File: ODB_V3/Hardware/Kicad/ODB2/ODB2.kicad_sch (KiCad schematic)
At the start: 95 parts, among them U1 STM32F412ZGTx, Y1 ABM8G-25.000MHZ-18-D2Y-T

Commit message: wip: route qspi
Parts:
- BARO_R1, BARO_R2, BARO_R3, BT_R3, Crystal_R1, EXTEND_R1, EXTEND_R10, EXTEND_R11, EXTEND_R2, EXTEND_R3, EXTEND_R4, EXTEND_R5, EXTEND_R6, EXTEND_R7, EXTEND_R8, EXTEND_R9, GPS_R1, IMU_R5, MEM_R1, MEM_R2, MEM_R3, MEM_R4, MEM_R5, MEM_R6, PA_R6, P_R21, P_R22, P_R23, P_R24, RFD_R1, SD_R1, SD_R2, SD_R3: footprint Resistor_SMD:R_0603_1608Metric -> Resistor_SMD:R_0402_1005Metric
- Crystal_C1, Crystal_C2: footprint Capacitor_SMD:C_0603_1608Metric -> Capacitor_SMD:C_0402_1005Metric
- Crystal_R2: value 1MHz -> 1M; footprint Resistor_SMD:R_0603_1608Metric -> Resistor_SMD:R_0402_1005Metric
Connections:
- net PH1: no longer Crystal_R2.2
- net at Crystal_C2.1, Crystal_R1.2, Y1.3: now also Crystal_R2.2
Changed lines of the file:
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@@
 	)
 	(junction
-		(at 391.16 127)
-		(diameter 0)
-		(color 0 0 0 0)
-	)
-	(junction
 		(at 210.82 44.45)
 		(diameter 0)
@@
 	)
 	(junction
+		(at 384.81 139.7)
+		(diameter 0)
+		(color 0 0 0 0)
+	)
+	(junction
 		(at 360.68 101.6)
 		(diameter 0)
@@
 	(wire
 		(pts
-			(xy 391.16 125.73) (xy 391.16 127)
-		)
-		(stroke
-			(width 0)
-			(type default)
-		)
-	)
-	(wire
-		(pts
 			(xy 147.32 213.36) (xy 147.32 218.44)
 		)
@@
 	(wire
 		(pts
-			(xy 381 139.7) (xy 391.16 139.7)
+			(xy 381 139.7) (xy 384.81 139.7)
 		)
 		(stroke
@@
 	(wire
 		(pts
-			(xy 364.49 127) (xy 391.16 127)
-		)
-		(stroke
-			(width 0)
-			(type default)
-		)
-	)
-	(wire
-		(pts
 			(xy 147.32 55.88) (xy 147.32 57.15)
 		)
@@
 	(wire
 		(pts
+			(xy 384.81 139.7) (xy 391.16 139.7)
+		)
+		(stroke
+			(width 0)
+			(type default)
+		)
+	)
+	(wire
+		(pts
+			(xy 364.49 127) (xy 384.81 127)
+		)
+		(stroke
+			(width 0)
+			(type default)
+		)
+	)
+	(wire
+		(pts
 			(xy 365.76 26.67) (xy 365.76 31.75)
 		)
@@
 	(wire
 		(pts
-			(xy 391.16 127) (xy 391.16 129.54)
+			(xy 391.16 125.73) (xy 391.16 129.54)
 		)
 		(stroke
@@
 	(wire
 		(pts
+			(xy 384.81 127) (xy 384.81 139.7)
+		)
+		(stroke
+			(width 0)
+			(type default)
+		)
+	)
+	(wire
+		(pts
 			(xy 388.62 31.75) (xy 388.62 34.29)
 		)
@@
 			)
 		)
-		(property "Footprint" "Resistor_SMD:R_0603_1608Metric"
+		(property "Footprint" "Resistor_SMD:R_0402_1005Metric"
 			(at 163.83 158.242 90)
 			(effects
@@
 			)
 		)
-		(property "Footprint" "Resistor_SMD:R_0603_1608Metric"
+		(property "Footprint" "Resistor_SMD:R_0402_1005Metric"
 			(at 238.76 189.738 90)
 			(effects
@@
 			)
 		)
-		(property "Footprint" "Resistor_SMD:R_0603_1608Metric"
+		(property "Footprint" "Resistor_SMD:R_0402_1005Metric"
 			(at 163.83 160.782 90)
 			(effects
@@
 			)
 		)
-		(property "Footprint" "Resistor_SMD:R_0603_1608Metric"
+		(property "Footprint" "Resistor_SMD:R_0402_1005Metric"
 			(at 237.49 70.358 90)
 			(effects
@@
 			)
 		)
-		(property "Footprint" "Resistor_SMD:R_0603_1608Metric"
+		(property "Footprint" "Resistor_SMD:R_0402_1005Metric"
 			(at 238.76 199.898 90)
 			(effects
@@
 			)
 		)
-		(property "Value" "1MHz"
+		(property "Value" "1M"
 			(at 360.68 124.714 90)
 			(effects
@@
 			)
 		)
-		(property "Footprint" "Resistor_SMD:R_0603_1608Metric"
+		(property "Footprint" "Resistor_SMD:R_0402_1005Metric"
 			(at 360.68 128.778 90)
 			(effects
@@
 			)
 		)
-		(property "Footprint" "Resistor_SMD:R_0603_1608Metric"
+		(property "Footprint" "Resistor_SMD:R_0402_1005Metric"
 			(at 237.49 113.538 90)
 			(effects
@@
 			)
 		)
-		(property "Footprint" "Resistor_SMD:R_0603_1608Metric"
+		(property "Footprint" "Resistor_SMD:R_0402_1005Metric"
 			(at 163.83 163.322 90)
 			(effects
@@
 			)
 		)
-		(property "Footprint" "Resistor_SMD:R_0603_1608Metric"
+		(property "Footprint" "Resistor_SMD:R_0402_1005Metric"
 			(at 237.49 75.438 90)
 			(effects
@@
 			)
 		)
-		(property "Footprint" "Resistor_SMD:R_0603_1608Metric"
+		(property "Footprint" "Resistor_SMD:R_0402_1005Metric"
 			(at 237.49 159.258 90)
 			(effects
@@
 			)
 		)
-		(property "Footprint" "Resistor_SMD:R_0603_1608Metric"
+		(property "Footprint" "Resistor_SMD:R_0402_1005Metric"
 			(at 163.83 196.342 90)
 			(effects
@@
 			)
 		)
-		(property "Footprint" "Capacitor_SMD:C_0603_1608Metric"
+		(property "Footprint" "Capacitor_SMD:C_0402_1005Metric"
 			(at 333.7052 144.78 0)
 			(effects
@@
 			)
 		)
-		(property "Footprint" "Capacitor_SMD:C_0603_1608Metric"
+		(property "Footprint" "Capacitor_SMD:C_0402_1005Metric"
 			(at 392.1252 148.59 0)
 			(effects
@@
 			)
 		)
-		(property "Footprint" "Resistor_SMD:R_0603_1608Metric"
+		(property "Footprint" "Resistor_SMD:R_0402_1005Metric"
 			(at 238.76 212.598 90)
 			(effects
@@
 			)
 		)
-		(property "Footprint" "Resistor_SMD:R_0603_1608Metric"
+		(property "Footprint" "Resistor_SMD:R_0402_1005Metric"
 			(at 163.83 148.082 90)
 			(effects
@@
 			)
 		)
-		(property "Footprint" "Resistor_SMD:R_0603_1608Metric"
+		(property "Footprint" "Resistor_SMD:R_0402_1005Metric"
 			(at 163.83 140.462 90)
 			(effects
@@
 			)
 		)
-		(property "Footprint" "Resistor_SMD:R_0603_1608Metric"
+		(property "Footprint" "Resistor_SMD:R_0402_1005Metric"
 			(at 237.49 138.938 90)
 			(effects
@@
 			)
 		)
-		(property "Footprint" "Resistor_SMD:R_0603_1608Metric"
+		(property "Footprint" "Resistor_SMD:R_0402_1005Metric"
 			(at 237.49 62.738 90)
 			(effects
@@
 			)
 		)
-		(property "Footprint" "Resistor_SMD:R_0603_1608Metric"
+		(property "Footprint" "Resistor_SMD:R_0402_1005Metric"
 			(at 389.382 133.35 90)
 			(effects
@@
 			)
 		)
-		(property "Footprint" "Resistor_SMD:R_0603_1608Metric"
+		(property "Footprint" "Resistor_SMD:R_0402_1005Metric"
 			(at 238.76 210.058 90)
 			(effects
@@
 			)
 		)
-		(property "Footprint" "Resistor_SMD:R_0603_1608Metric"
+		(property "Footprint" "Resistor_SMD:R_0402_1005Metric"
 			(at 163.83 82.042 90)
 			(effects
@@
 			)
 		)
-		(property "Footprint" "Resistor_SMD:R_0603_1608Metric"
+		(property "Footprint" "Resistor_SMD:R_0402_1005Metric"
 			(at 163.83 143.002 90)
 			(effects
@@
 			)
 		)
-		(property "Footprint" "Resistor_SMD:R_0603_1608Metric"
+		(property "Footprint" "Resistor_SMD:R_0402_1005Metric"
 			(at 163.83 198.882 90)
 			(effects
@@
 			)
 		)
-		(property "Footprint" "Resistor_SMD:R_0603_1608Metric"
+		(property "Footprint" "Resistor_SMD:R_0402_1005Metric"
 			(at 163.83 84.582 90)
 			(effects
@@
 			)
 		)
-		(property "Footprint" "Resistor_SMD:R_0603_1608Metric"
+		(property "Footprint" "Resistor_SMD:R_0402_1005Metric"
 			(at 237.49 126.238 90)
 			(effects
@@
 			)
 		)
-		(property "Footprint" "Resistor_SMD:R_0603_1608Metric"
+		(property "Footprint" "Resistor_SMD:R_0402_1005Metric"
 			(at 163.83 97.282 90)
 			(effects
@@
 			)
 		)
-		(property "Footprint" "Resistor_SMD:R_0603_1608Metric"
+		(property "Footprint" "Resistor_SMD:R_0402_1005Metric"
 			(at 238.76 192.278 90)
 			(effects
@@
 			)
 		)
-		(property "Footprint" "Resistor_SMD:R_0603_1608Metric"
+		(property "Footprint" "Resistor_SMD:R_0402_1005Metric"
 			(at 163.83 145.542 90)
 			(effects
@@
 			)
 		)
-		(property "Footprint" "Resistor_SMD:R_0603_1608Metric"
+		(property "Footprint" "Resistor_SMD:R_0402_1005Metric"
 			(at 237.49 67.818 90)
 			(effects
@@
 			)
 		)
-		(property "Footprint" "Resistor_SMD:R_0603_1608Metric"
+		(property "Footprint" "Resistor_SMD:R_0402_1005Metric"
 			(at 163.83 203.962 90)
 			(effects
@@
 			)
 		)
-		(property "Footprint" "Resistor_SMD:R_0603_1608Metric"
+		(property "Footprint" "Resistor_SMD:R_0402_1005Metric"
 			(at 238.76 207.518 90)
 			(effects
@@
 			)
 		)
-		(property "Footprint" "Resistor_SMD:R_0603_1608Metric"
+		(property "Footprint" "Resistor_SMD:R_0402_1005Metric"
 			(at 238.76 194.818 90)
 			(effects
@@
 			)
 		)
-		(property "Footprint" "Resistor_SMD:R_0603_1608Metric"
+		(property "Footprint" "Resistor_SMD:R_0402_1005Metric"
 			(at 237.49 133.858 90)
 			(effects
@@
 			)
 		)
-		(property "Footprint" "Resistor_SMD:R_0603_1608Metric"
+		(property "Footprint" "Resistor_SMD:R_0402_1005Metric"
 			(at 237.49 103.378 90)
 			(effects
@@
 			)
 		)
-		(property "Footprint" "Resistor_SMD:R_0603_1608Metric"
+		(property "Footprint" "Resistor_SMD:R_0402_1005Metric"
 			(at 238.76 197.358 90)
 			(effects
@@
 			)
 		)
-		(property "Footprint" "Resistor_SMD:R_0603_1608Metric"
+		(property "Footprint" "Resistor_SMD:R_0402_1005Metric"
 			(at 237.49 80.518 90)
 			(effects

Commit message: WIP : routing pyros et interfaces communications
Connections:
- net Fire_1: now also P_R24.2; no longer P_R21.2
- net Fire_2: now also P_R23.2; no longer P_R22.2
- net Fire_3: now also P_R22.2; no longer P_R23.2
- net Fire_4: now also P_R21.2; no longer P_R24.2
- net Sense_1: now also U1.46 (PB0); no longer U1.35 (PA1)
- net Sense_2: now also U1.45 (PC5); no longer U1.44 (PC4)
- net Sense_3: now also U1.44 (PC4); no longer U1.45 (PC5)
- net Sense_4: now also U1.35 (PA1); no longer U1.46 (PB0)

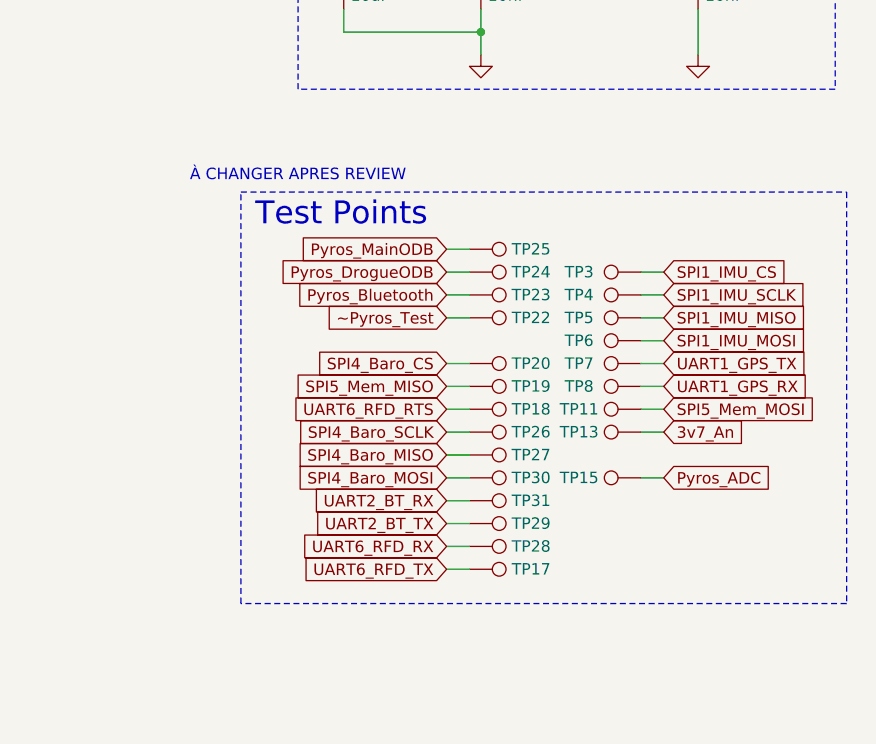
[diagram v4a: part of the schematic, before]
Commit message: wip: trace temperature sensor +  add extend_IO exclusion (missing) + fix/modification components traces/position and convert some 7.85mils -> 10mils + add ODBlix and version Silkscreen + trace criticalLED + remove testpads (add later)
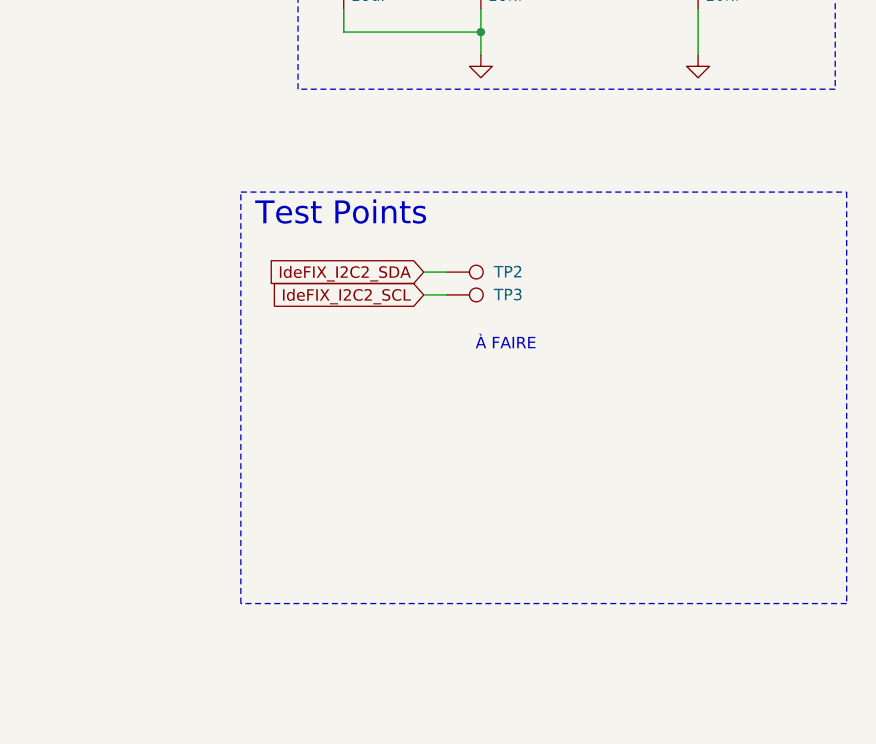
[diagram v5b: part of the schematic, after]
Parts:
- removed TP11, TP13, TP15, TP17, TP18, TP19, TP20, TP22, TP23, TP24, TP25, TP26, TP27, TP28, TP29, TP30, TP31, TP4, TP5, TP6, TP7, TP8: TestPoint, TestPoint:TestPoint_Pad_D1.0mm, symbol Connector:TestPoint
- added TP3: TestPoint, TestPoint:TestPoint_Pad_D1.0mm, symbol Connector:TestPoint
- EXTEND_R10, EXTEND_R11, EXTEND_R8, EXTEND_R9: now in the parts list
- renumbered TP3 to TP2
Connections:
- net SPI1_IMU_CS is gone; now on net IdeFIX_I2C2_SDA: TP2.1
- net IdeFIX_I2C2_SCL: now also TP3.1
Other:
- note added: "À FAIRE"
- note removed: "À CHANGER APRES REVIEW"
- moved on the sheet: TP2

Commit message: wip: fix chainfreiner zone
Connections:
- net BT_USART2_RX: now also TP3.1
- net BT_USART2_TX: now also TP2.1
- net IdeFIX_I2C2_SCL: no longer TP3.1
- net IdeFIX_I2C2_SDA: no longer TP2.1
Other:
- note removed: "À FAIRE"
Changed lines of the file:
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@@
 		)
 	)
-	(text "À FAIRE"
-		(exclude_from_sim no)
-		(at 368.554 222.758 0)
-		(effects
-			(font
-				(size 1.27 1.27)
-			)
-		)
-	)
 	(junction
 		(at 187.96 44.45)
@@
 		)
 	)
-	(global_label "IdeFIX_I2C2_SCL"
+	(global_label "BT_USART2_RX"
 		(shape input)
 		(at 359.41 217.17 180)
@@
 		)
 		(property "Intersheetrefs" "${INTERSHEET_REFS}"
-			(at 340.9429 217.17 0)
+			(at 342.6968 217.17 0)
 			(effects
 				(font
@@
 		)
 	)
-	(global_label "IdeFIX_I2C2_SDA"
+	(global_label "BT_USART2_TX"
 		(shape input)
 		(at 359.41 214.63 180)
@@
 		)
 		(property "Intersheetrefs" "${INTERSHEET_REFS}"
-			(at 340.8824 214.63 0)
+			(at 342.9992 214.63 0)
 			(effects
 				(font

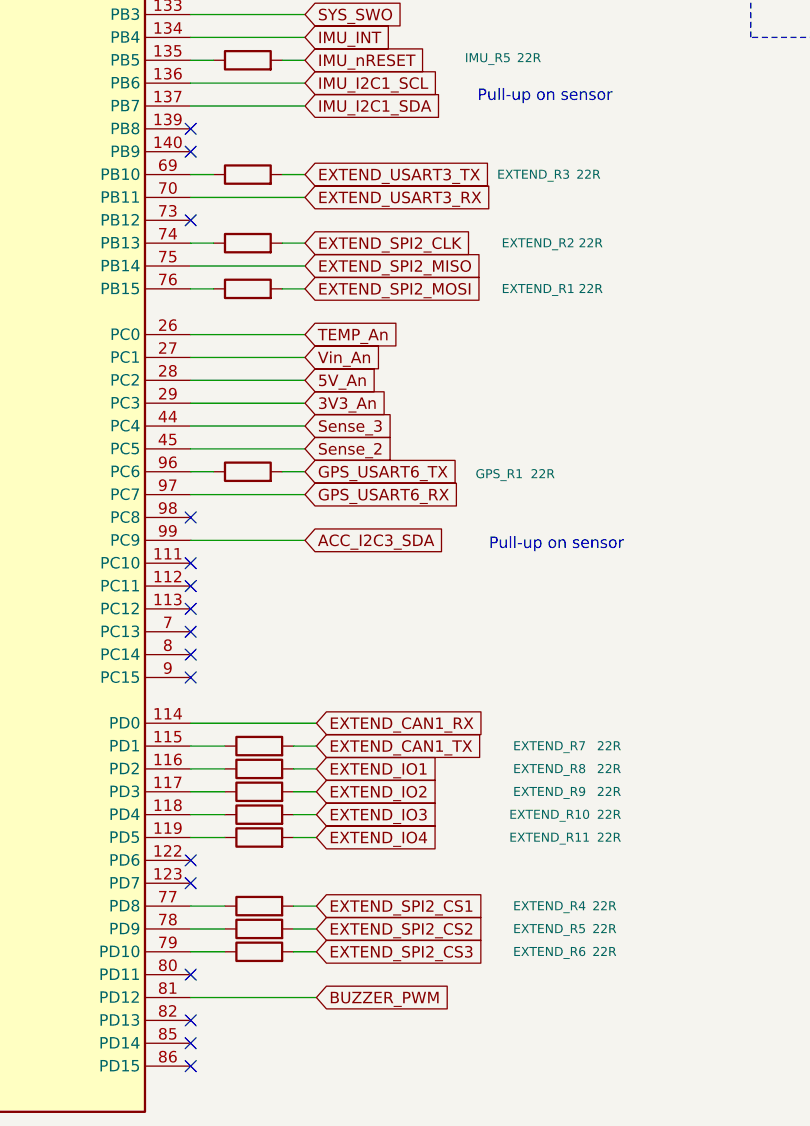
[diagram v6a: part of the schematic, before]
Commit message: wip: change extendio to function (include uart3) + fix corner + modify stm32cubeide ico to fit with kicad
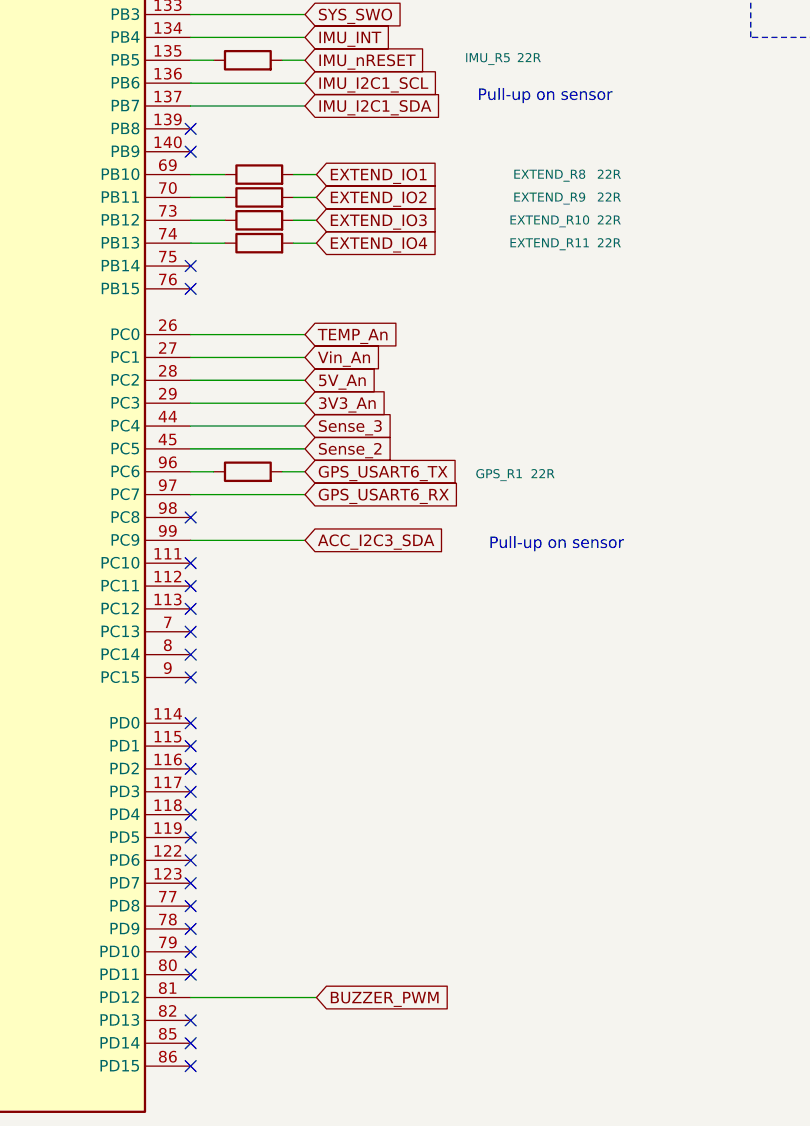
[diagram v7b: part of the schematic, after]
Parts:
- removed EXTEND_R1, EXTEND_R2, EXTEND_R3, EXTEND_R4, EXTEND_R5, EXTEND_R6, EXTEND_R7: 22R, Resistor_SMD:R_0402_1005Metric, symbol Device:R
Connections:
- net at EXTEND_R11.1: now also U1.74 (PB13); no longer U1.119 (PD5)
- net at U1.69 (PB10): now also EXTEND_R8.1
- net at U1.116 (PD2): no longer EXTEND_R8.1
- net at U1.117 (PD3): no longer EXTEND_R9.1
- net at U1.118 (PD4): no longer EXTEND_R10.1
- net at U1.73 (PB12): now also EXTEND_R10.1
- net EXTEND_CAN1_RX: no longer names the net of U1.114 (PD0)
- net EXTEND_SPI2_MISO: no longer names the net of U1.75 (PB14)
- net EXTEND_USART3_RX: no longer names the net of U1.70 (PB11)
- net EXTEND_USART3_RX: now also EXTEND_R9.1
- no-connect marks 45 -> 55
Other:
- moved on the sheet: EXTEND_R10, EXTEND_R11, EXTEND_R8, EXTEND_R9

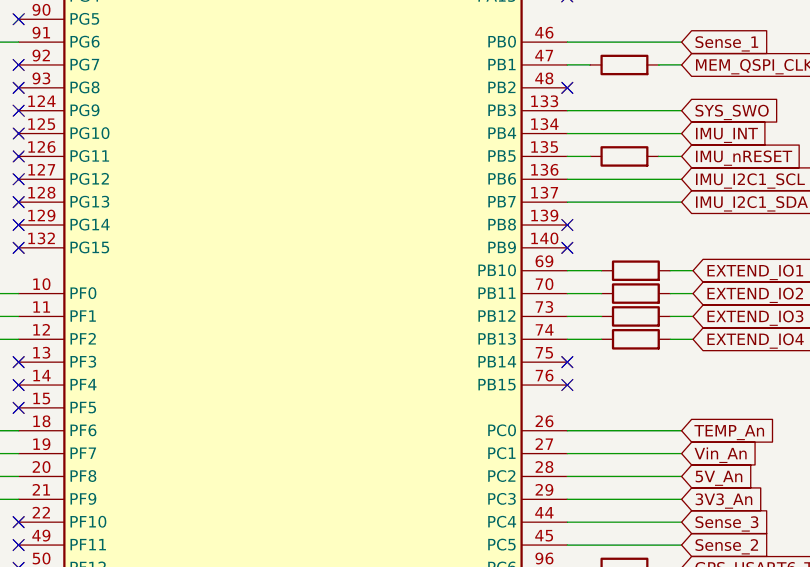
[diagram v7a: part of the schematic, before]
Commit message: wip: add silkscreen + add missing 3D models
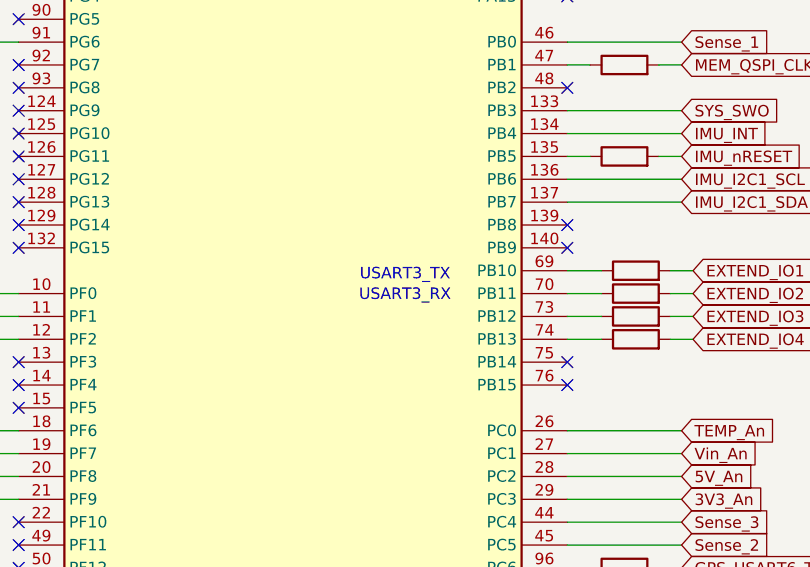
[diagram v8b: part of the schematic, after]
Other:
- note added: "USART3_RX"
- note added: "USART3_TX"
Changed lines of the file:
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@@
+		)
+	)
+	(text "USART3_TX"
+		(exclude_from_sim no)
+		(at 213.106 124.968 0)
+		(effects
+			(font
+				(size 1.27 1.27)
+			)
 		)
 	)
@@
 		(effects
 			(font
+				(size 1.27 1.27)
+			)
+		)
+	)
+	(text "USART3_RX"
+		(exclude_from_sim no)
+		(at 213.106 127.254 0)
+		(effects
+			(font
